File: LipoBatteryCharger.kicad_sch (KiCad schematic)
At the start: 28 parts, among them Q1 2N3906, Q3 PMOS, U1 LM741, U2 LM393, U4 74HC02, U6 TL431LP, U7 TL431LP

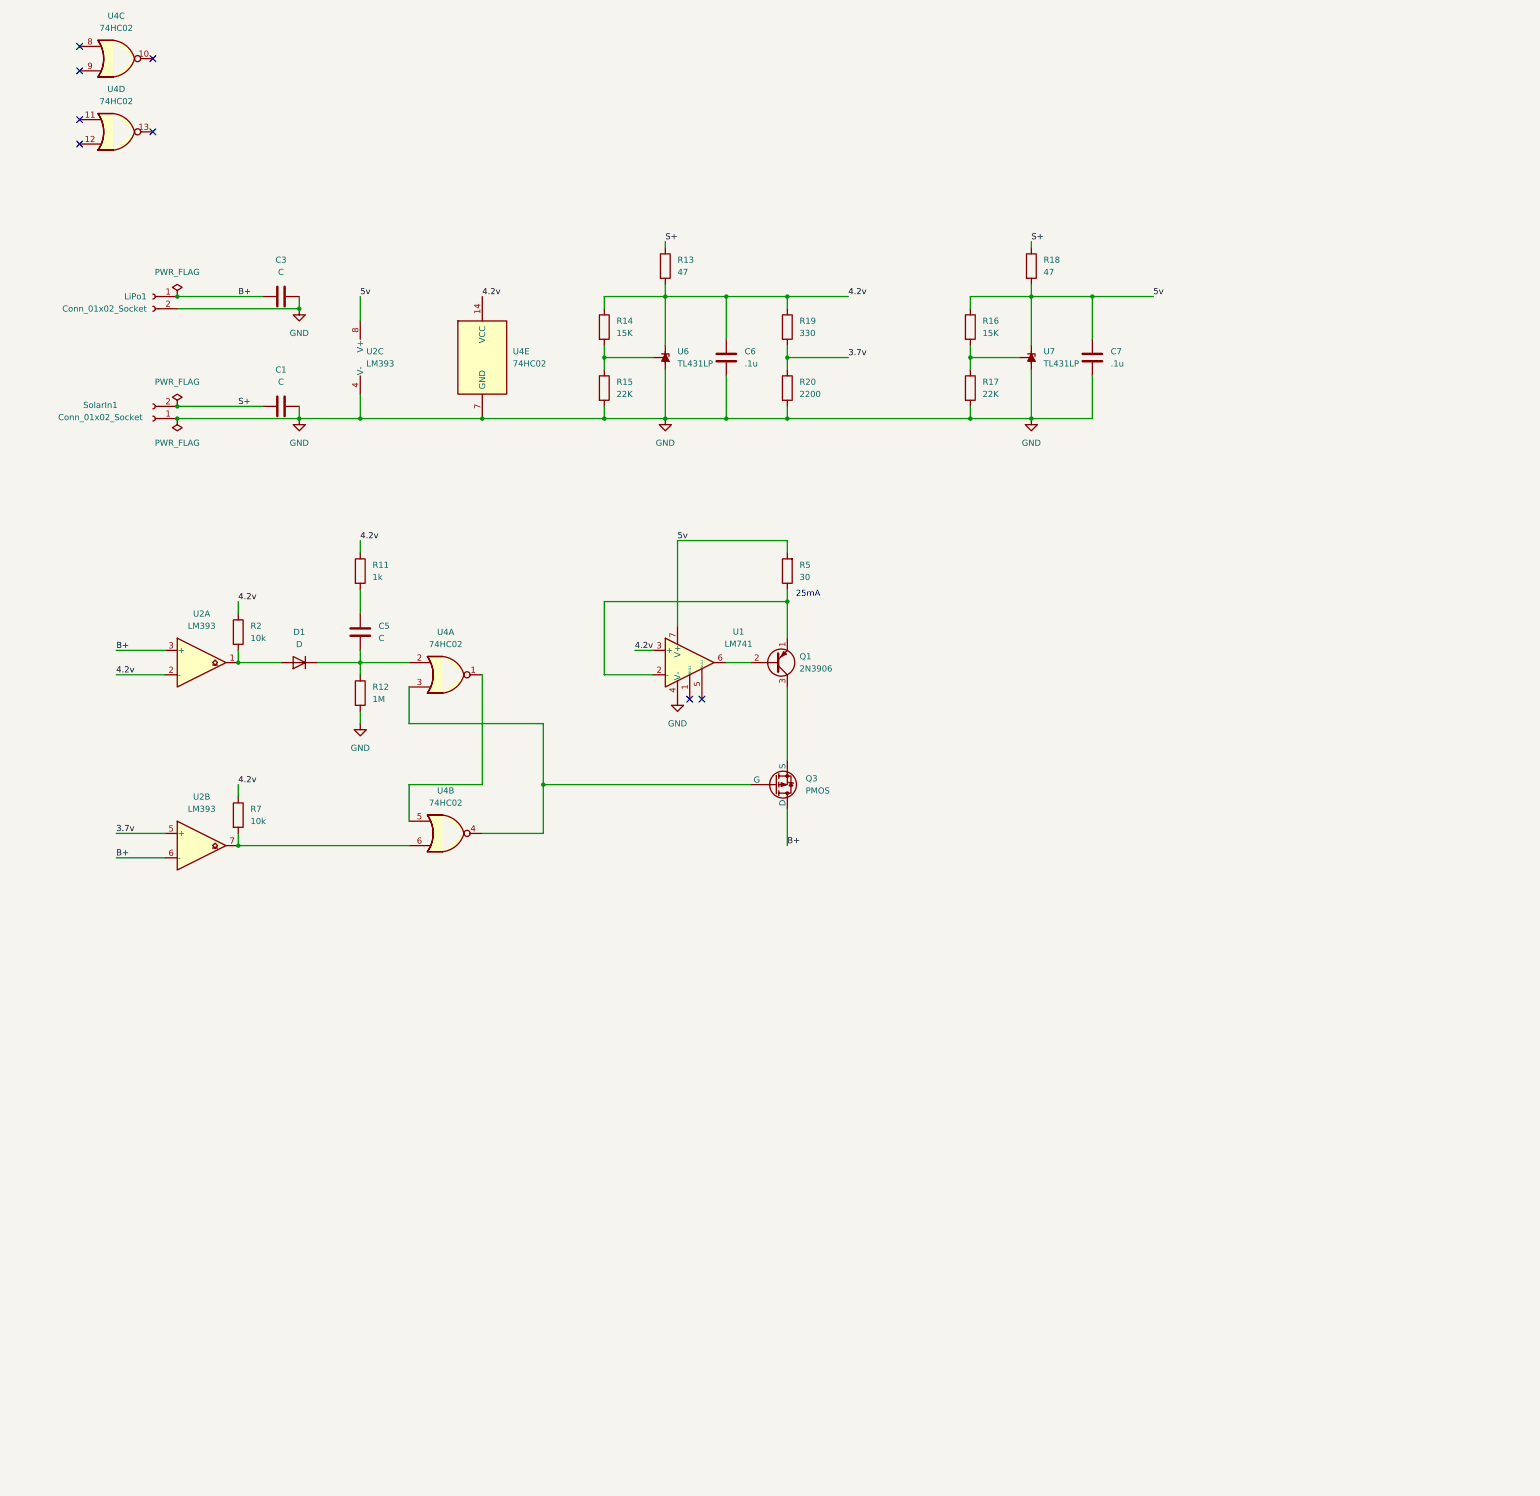
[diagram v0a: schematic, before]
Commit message: Implemented trickle charge and constant current switching logic
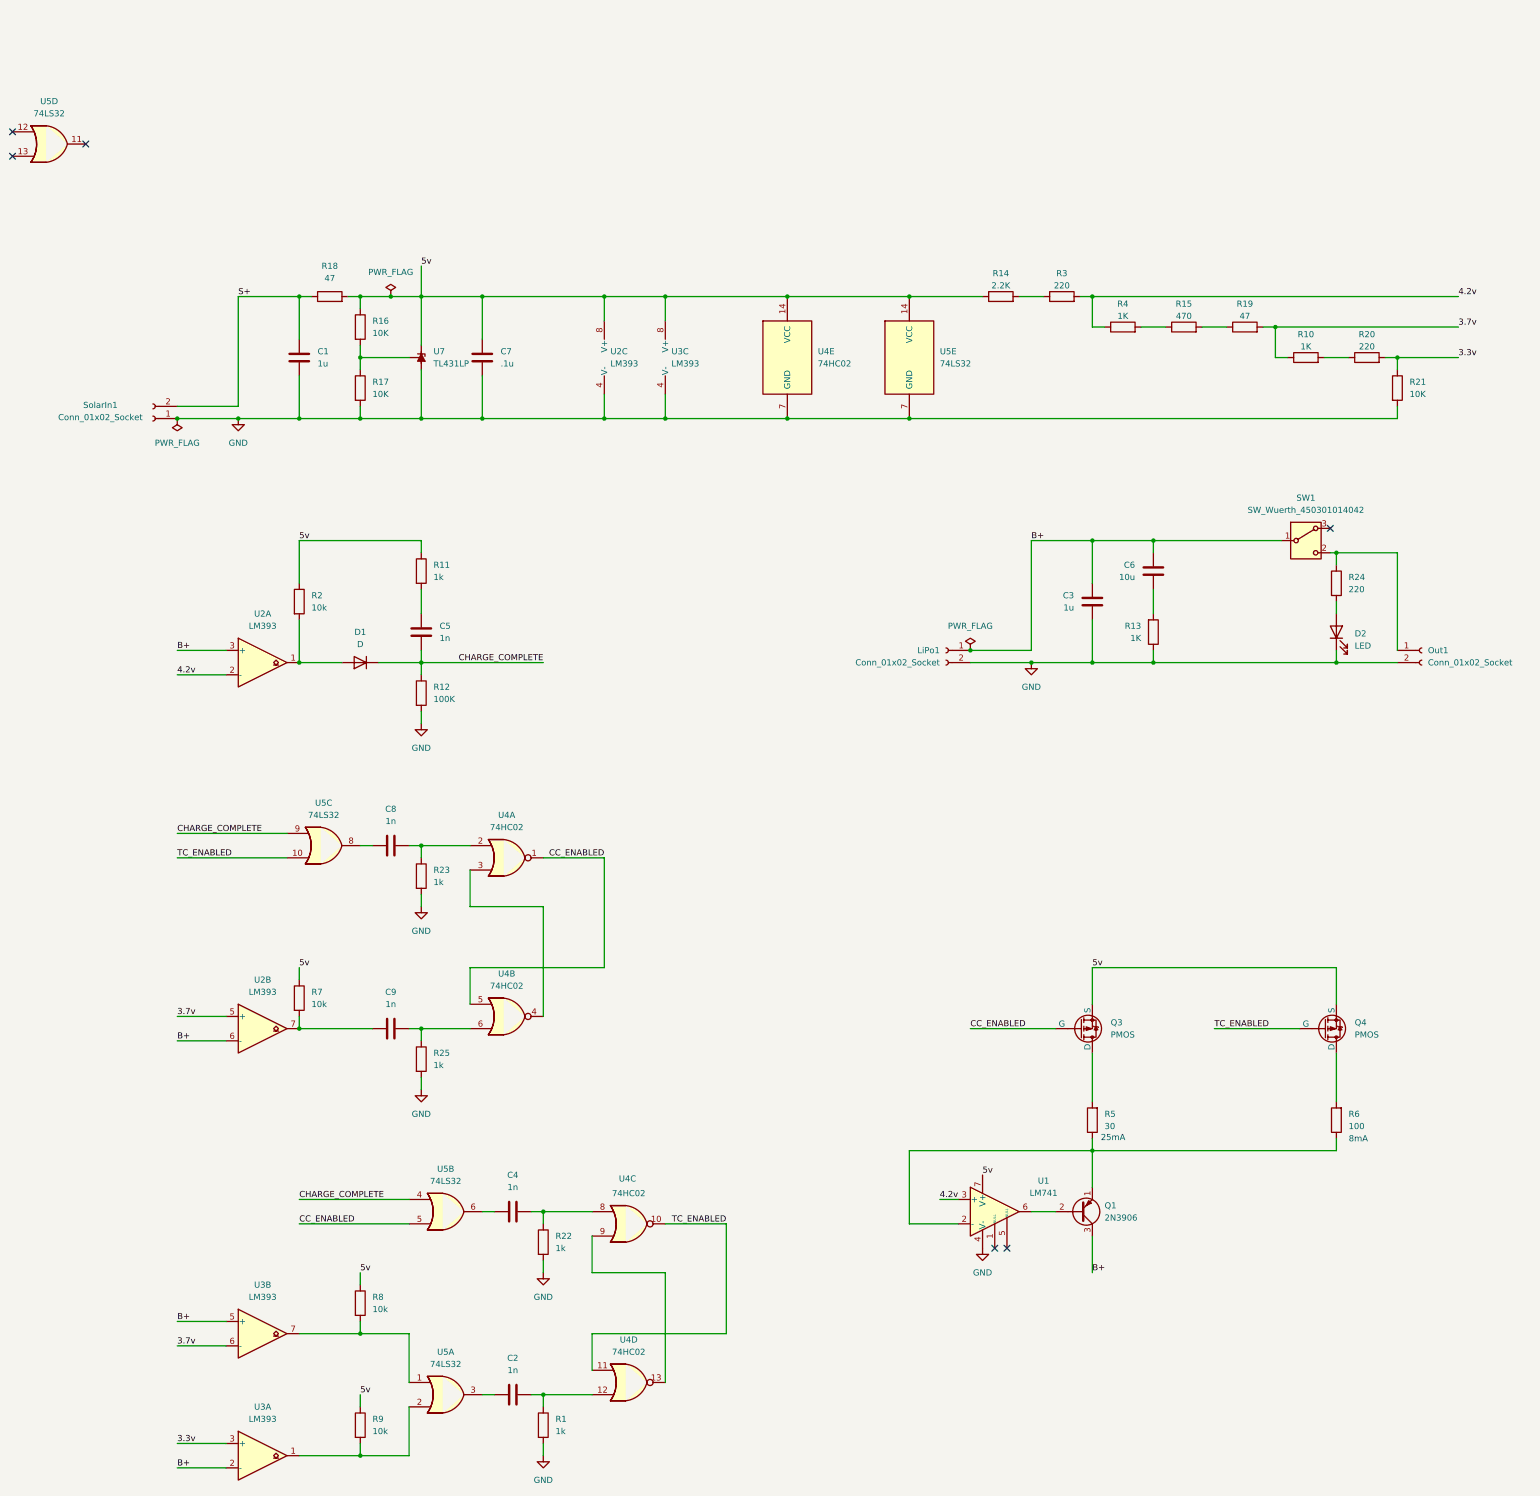
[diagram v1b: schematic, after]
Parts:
- removed U6: TL431LP, Package_TO_SOT_THT:TO-92_Inline, symbol Reference_Voltage:TL431LP
- added C2, C4, C8, C9: 1n, symbol Device:C
- added D2: LED, symbol Device:LED
- added Out1: Conn_01x02_Socket, symbol Connector:Conn_01x02_Socket
- added Q4: PMOS, symbol Simulation_SPICE:PMOS
- added R1, R22, R23, R25: 1k, symbol Device:R
- added R10, R4: 1K, symbol Device:R
- added R21: 10K, symbol Device:R
- added R24, R3: 220, symbol Device:R
- added R6: 100, symbol Device:R
- added R8, R9: 10k, symbol Device:R
- added SW1: SW_Wuerth_450301014042, Button_Switch_THT:SW_Slide-03_Wuerth-WS-SLTV_10x2.5x6.4_P2.54mm, symbol Switch:SW_Wuerth_450301014042
- added U3: LM393, symbol Comparator:LM393
- added U5: 74LS32, symbol 74xx:74LS32
- C1, C3: value C -> 1u
- C5: value C -> 1n
- C6: value .1u -> 10u
- R12: value 1M -> 100K
- R13: value 47 -> 1K
- R14: value 15K -> 2.2K
- R15: value 22K -> 470
- R16: value 15K -> 10K
- R17: value 22K -> 10K
- R19: value 330 -> 47
- R20: value 2200 -> 220
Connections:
- net 3.7v: now also R10.1, U3.6 (-); no longer R20.1
- net 4.2v: now also R3.2, R4.1; no longer C6.1, R11.1, R13.2, R14.1, R19.1, R2.1, R7.1, U4.14 (VCC)
- net 5v: now also Q3.3 (S), R11.1, R14.1, R2.1, R7.1, U4.14 (VCC), Q4.3 (S), R8.1, R9.1, U3.8 (V+), U5.14 (VCC); no longer R5.2
- net B+: now also C6.1, Q1.3 (C), SW1.1 (B), U3.2 (-), U3.5 (+); no longer Q3.1 (D)
- net GND: now also C1.1, R13.1, D2.1 (K), Out1.2 (Pin_2), R1.2, R21.2, R22.2, R23.2, R25.2, U3.4 (V-), U5.7 (GND); no longer C1.2, C6.2, R15.2, R20.2
- net S+: now also C1.2; no longer C1.1, R13.1
- net at R7.2, U2.7: now also C9.1; no longer U4.6
- net CHARGE_COMPLETE: now reaches C5.2, D1.1 (K), R12.1
- net CHARGE_COMPLETE: now also U5.4, U5.9; no longer U4.2
- net TC_ENABLED: now reaches U4.11
- net TC_ENABLED: now also U4.10, Q4.2 (G), U5.10
- net at U4.12: now also C2.2, R1.1
- net at U4.13: now also U4.9
- net CC_ENABLED: now reaches U4.1, U4.5
- net CC_ENABLED: now also Q3.2 (G), U5.5
- net at U4.3, U4.4: no longer Q3.2 (G)
- net at R14.2: now also R3.1; no longer R15.1
- net at Q1.1 (E), R5.1, U1.2 (-): now also R6.1
- net at U4.8: now also C4.2, R22.1
- new net: Q4.1 (D), R6.2
- new net: C9.2, R25.1, U4.6
- new net: R8.2, U3.7, U5.1
- new net: R9.2, U3.1, U5.2
- new net: C2.1, U5.3
- new net: C8.1, U5.8
- new net: C6.2, R13.2
- new net: C8.2, R23.1, U4.2
- new net: D2.2 (A), R24.2
- new net: R15.1, R4.2
- new net: C4.1, U5.6
- new net: Out1.1 (Pin_1), R24.1, SW1.2 (C)
- new net: R15.2, R19.1
- new net: Q3.1 (D), R5.2
- new net: R10.2, R20.1
- new net 3.3v: R20.2, R21.1, U3.3 (+)
- no-connect marks 8 -> 6
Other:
- note added: "8mA"
- moved on the sheet: C3, C5, C7, D1, LiPo1, Q1, Q3, R11, R12, R16, R17, R2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

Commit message: Reordered pulses on differentials
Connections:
- net CC_ENABLED: now also C4.1; no longer U5.5
- net TC_ENABLED: now also C8.1; no longer U5.10
- net at C4.2, R22.1: now also U5.5; no longer U4.8
- net at R8.2, U3.7: now also C2.1; no longer U5.1
- net at U5.3: now also U4.12; no longer C2.1
- net at U5.8: now also U4.2; no longer C8.1
- net at C2.2, R1.1: now also U5.1; no longer U4.12
- net at C8.2, R23.1: now also U5.10; no longer U4.2
- net at U5.6: now also U4.8; no longer C4.1
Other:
- moved on the sheet: C9, Q1, Q3, Q4, R25, R5, R6, R7, R8, R9, U1, U2B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

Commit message: Added diode to prevent leakage
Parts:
- added D3, D4, D5: D, symbol Device:D
- R5: value 30 -> 10
- R6: value 100 -> 33
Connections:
- net B+: now also D5.1 (K); no longer Q1.3 (C)
- net CC_ENABLED: no longer Q3.2 (G)
- net TC_ENABLED: no longer Q4.2 (G)
- net at R6.2: now also D4.1 (K); no longer Q4.1 (D)
- net ~{TC_ENABLED}: now reaches U4.13, U4.9
- net ~{TC_ENABLED}: now also Q4.2 (G)
- net ~{CC_ENABLED}: now reaches U4.3, U4.4
- net ~{CC_ENABLED}: now also Q3.2 (G)
- net at R5.2: now also D3.1 (K); no longer Q3.1 (D)
- new net: D4.2 (A), Q4.1 (D)
- new net: D3.2 (A), Q3.1 (D)
- new net: D5.2 (A), Q1.3 (C)
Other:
- note added: "20mA"
- note added: "6mA"
- note removed: "25mA"
- note removed: "8mA"
- moved on the sheet: Q3, Q4
